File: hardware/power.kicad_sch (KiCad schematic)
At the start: 0 parts

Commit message: train schematics
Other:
- company: Erdapfel -> Frisius
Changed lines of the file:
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@@
   (title_block
     (rev "A")
-    (company "Erdapfel")
+    (company "Frisius")
   )
   (hierarchical_label "VDD_CORE_EN" (shape input) (at 71.755 96.52 180)

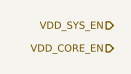
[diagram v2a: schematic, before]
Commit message: usb, bms, proc, btn changes
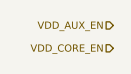
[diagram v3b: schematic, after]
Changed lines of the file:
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@@
     (effects (font (size 0.8 0.8)) (justify right))
   )
-  (hierarchical_label "VDD_SYS_EN" (shape input) (at 71.755 93.98 180)
+  (hierarchical_label "VDD_AUX_EN" (shape input) (at 71.755 93.98 180)
     (effects (font (size 0.8 0.8)) (justify right))
   )

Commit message: started b2b and power
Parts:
- added C? (x2): 4.7u, Capacitor_SMD:C_0603_1608Metric, symbol Device:C_Small
- added C? (x4): 0.1u, Capacitor_SMD:C_0603_1608Metric, symbol Device:C_Small
- added R? (x2): 10k, Resistor_SMD:R_0603_1608Metric, symbol Device:R_Small
- added R? (x2): 0, Resistor_SMD:R_0603_1608Metric, symbol Device:R_Small
- added U? (x2): LK112M33TR, Package_TO_SOT_SMD:SOT-23-5, symbol Regulator_Linear:LK112M33TR
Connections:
- new net: R?.1, U?.1 (SHDN) (x2)
- new net: C?.1, U?.3 (Bypass) (x2)
- new net: C?.1, R?.1, R?.1, R?.2, U?.5 (IN)
- new net GND: C?.2, C?.2, C?.2, C?.2, C?.2, C?.2, U?.2 (GND), U?.2 (GND)
- new net VBUS: R?.2
- new net VBUS_OVP: R?.2
- new net VCC_BKUP_3V3: C?.1, U?.4 (OUT)
- new net VDD_NVDC: C?.1, R?.2, U?.5 (IN)
- new net VDD_USB_3V3: C?.1, U?.4 (OUT)
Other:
- note added: "ISL9113A"
- note added: "NVC8187"
- note added: "Need to reduce 5-12V range to 3.3V, OVP needed, or VBUS from MCP77751 BYP."

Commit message: ready for first review
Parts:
- added C? (x6): 0.1u, Capacitor_SMD:C_0603_1608Metric, symbol Device:C_Small
- added C? (x13): 4.7u, Capacitor_SMD:C_0603_1608Metric, symbol Device:C_Small
- added D?: MBR0540, symbol Device:D_Zener_Small_Filled
- added D? (x3): LED_Small_Filled, symbol Device:LED_Small_Filled
- added L?: L_Small, symbol Device:L_Small
- added R? (x3): 1k, Resistor_SMD:R_0603_1608Metric, symbol Device:R_Small
- added R? (x6): 10k, Resistor_SMD:R_0603_1608Metric, symbol Device:R_Small
- added R?: 180k, Resistor_SMD:R_0603_1608Metric, symbol Device:R_Small
- added U? (x2): NCV8187AMLExCG, Package_DFN_QFN:DFN-8-1EP_3x3mm_P0.65mm_EP1.55x2.4mm, symbol bt_PMIC_Linear:NCV8187AMLExCG
- added U? (x2): PM8903A, Package_DFN_QFN:VQFN-16-1EP_3x3mm_P0.5mm_EP1.45x1.45mm_ThermalVias, symbol bt_PMIC_DCDC_Buck:PM8903A
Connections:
- net 3V3_CORE: now also C?.1, C?.1, D?.2 (A), U?.1 (OUT), U?.2 (SNS/ADJ)
- net GND: now also C?.1, C?.1, C?.2, C?.2, C?.2, C?.2, C?.2, C?.2, C?.2, C?.2, R?.2, R?.2, U?.5 (GND), U?.5 (GND), U?.9 (GND), U?.9 (GND)
- net VCC_BKUP_3V3: now also C?.1, C?.2, U?.12 (VCC)
- net VDD_AUX_3V3: now also C?.1, C?.1, D?.2 (A), U?.1 (OUT), U?.2 (SNS/ADJ)
- net VDD_AUX_EN: now also U?.7 (EN)
- net VDD_CORE_EN: now also D?.1 (K), R?.2, U?.1 (EN)
- net VDD_NVDC: now also C?.1, C?.1, C?.1, U?.13 (VIN), U?.14 (VIN)
- new net: D?.1 (K), R?.1 (x3)
- new net: R?.2, U?.3 (PG) (x2)
- new net: C?.1, C?.2, U?.11 (GND)
- new net: C?.1, R?.1 (x2)
- new net: C?.2, C?.2, R?.1, R?.2, R?.2, U?.10 (FB)
- new net: C?.1, C?.1, C?.1, C?.1, C?.2, C?.2, C?.2, D?.2 (A), L?.2, R?.1, R?.1, R?.2, U?.8 (IN), U?.8 (IN)
- new net: R?.1, U?.7 (EN)
- new net: R?.1, U?.8 (PSKIP/MS)
- new net: C?.1, R?.2, U?.9 (COMP)
- new net: C?.2, L?.1, U?.5 (PHASE), U?.6 (PHASE), U?.7 (PHASE)
- new net: C?.1, U?.4 (BOOT)
- new net: C?.2, C?.2, C?.2, U?.15 (PGND), U?.16 (PGND)
- new net: R?.2, U?.3 (PGOOD)
- new net CORE_BOOTSTRAP: D?.2 (A)
- no-connect marks 0 -> 1
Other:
- note added: "Aux controlled by MCU."
- note added: "Backup regulator always on"
- note added: "Bootstrap allows hard shutdown of core rail, startup via button or other source. Shutdown triggered by ESP pulling low."
- note added: "Core LDO acrive by default."
- note removed: "ISL9113A"
- note removed: "NVC8187"
- moved on the sheet: C?, R?, U?

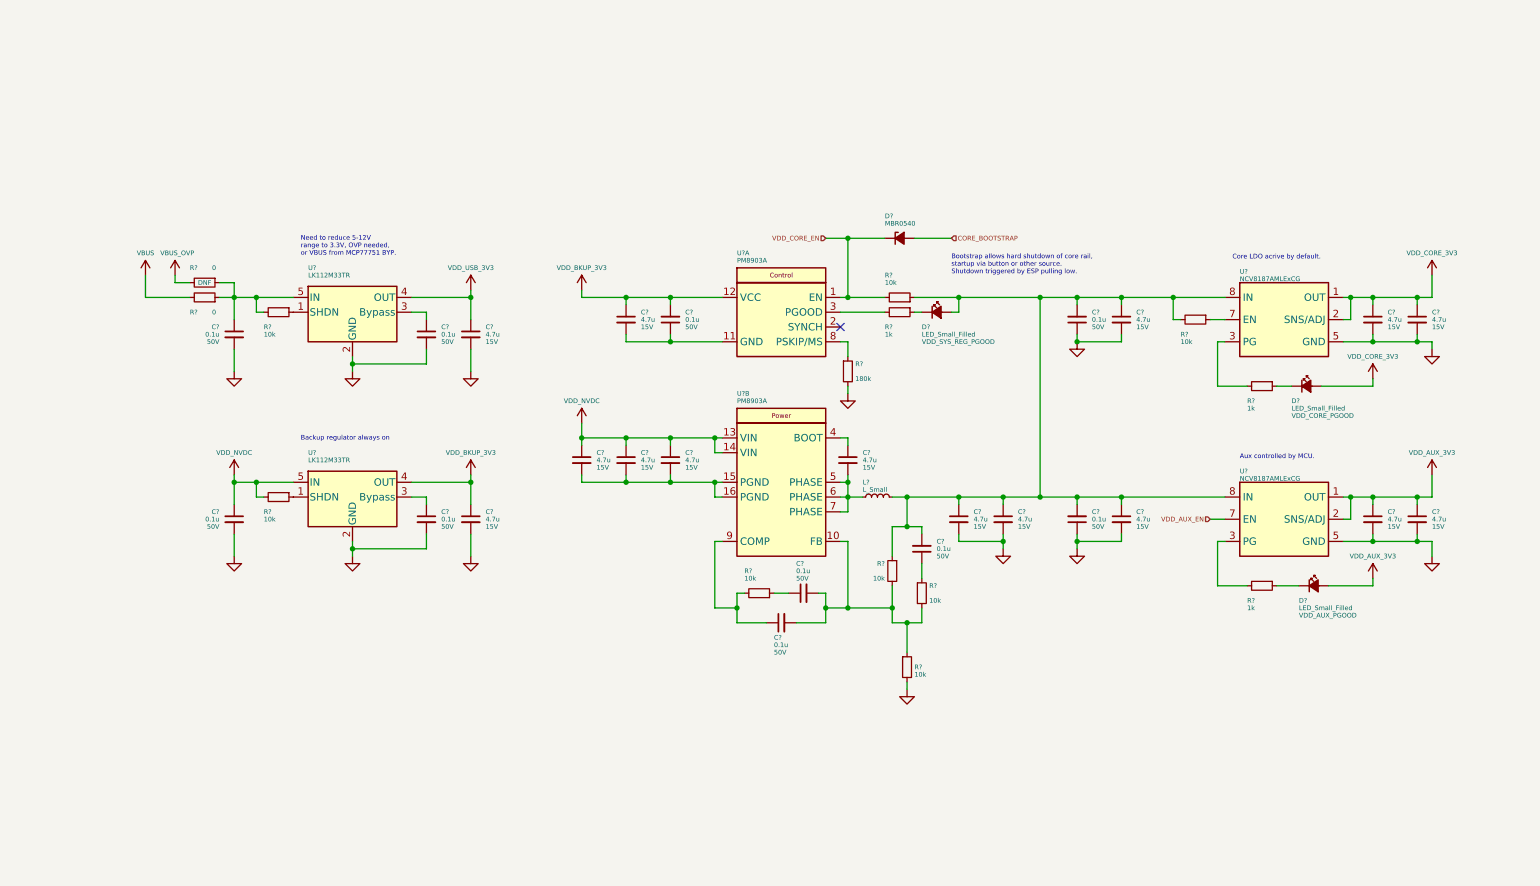
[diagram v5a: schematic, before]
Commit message: checking footprint assignment, added current sense pac1934 for dev
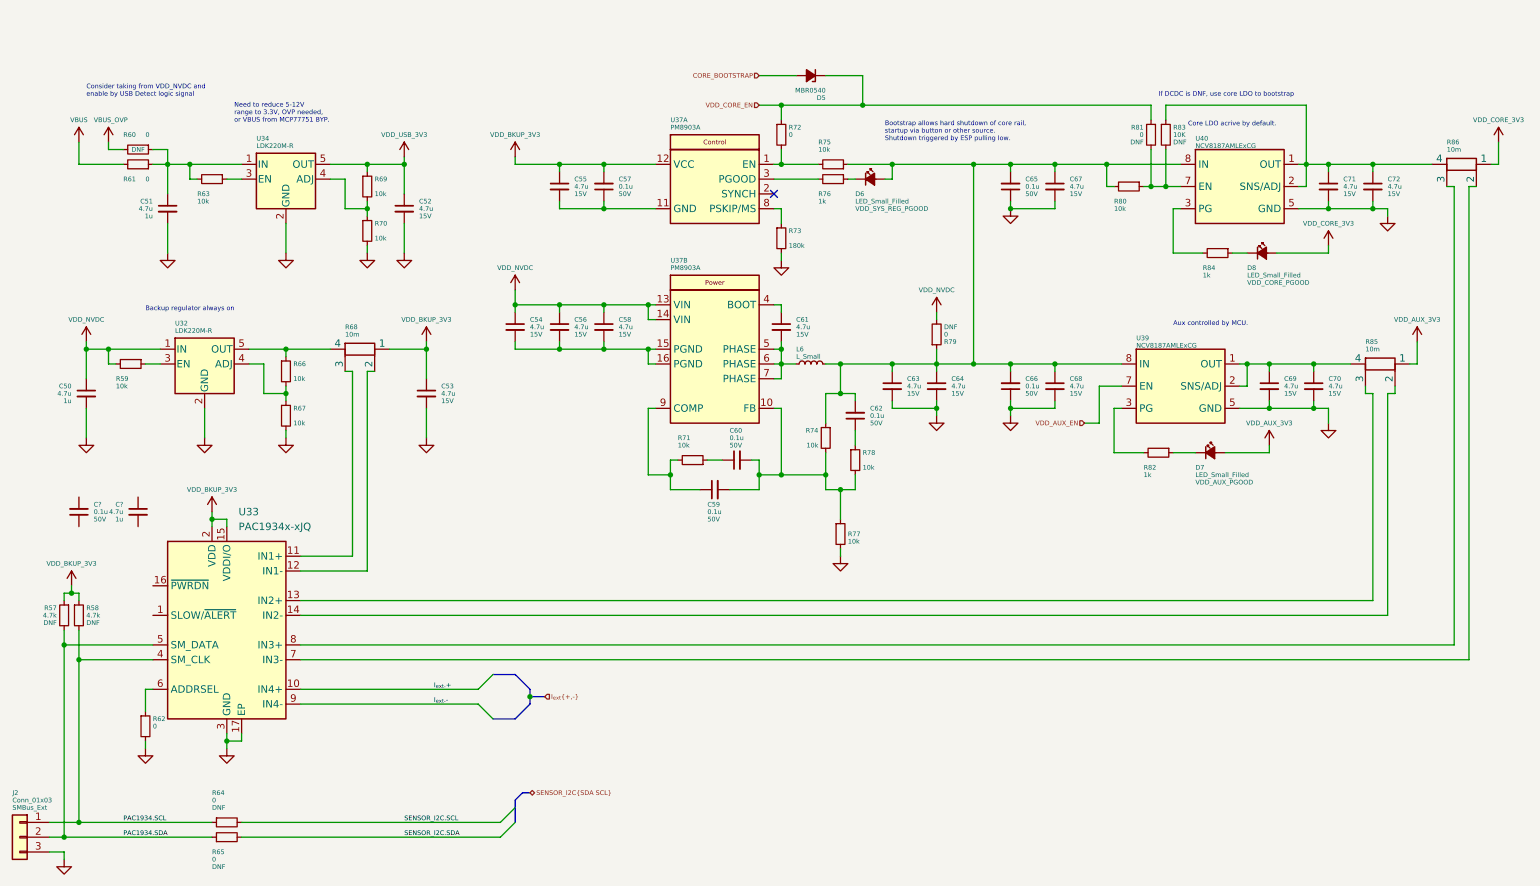
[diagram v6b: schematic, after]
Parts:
- removed C?: 4.7u, Capacitor_SMD:C_0603_1608Metric, symbol Device:C_Small
- removed C? (x4): 0.1u, Capacitor_SMD:C_0603_1608Metric, symbol Device:C_Small
- removed R?: 10k, Resistor_SMD:R_0603_1608Metric, symbol Device:R_Small
- removed U? (x2): LK112M33TR, Package_TO_SOT_SMD:SOT-23-5, symbol Regulator_Linear:LK112M33TR
- added C50, C51, C53, C?: 4.7u, Capacitor_SMD:C_0603_1608Metric, symbol Device:C_Small
- added C?: 0.1u, Capacitor_SMD:C_0603_1608Metric, symbol Device:C_Small
- added J2: Conn_01x03, Connector_PinHeader_1.00mm:PinHeader_1x03_P1.00mm_Vertical, symbol Connector_Generic:Conn_01x03
- added R57, R58: 4.7k, Resistor_SMD:R_0603_1608Metric, symbol Device:R_Small
- added R59, R66, R67, R69, R70: 10k, Resistor_SMD:R_0603_1608Metric, symbol Device:R_Small
- added R62, R64, R65, R72, R79, R81: 0, Resistor_SMD:R_0603_1608Metric, symbol Device:R_Small
- added R68, R85, R86: 10m, Resistor_SMD:R_1210_3225Metric, symbol Device:R_Shunt
- added R83: 10K, Resistor_SMD:R_0603_1608Metric, symbol Device:R_Small
- added U32, U34: LDK220M-R, Package_TO_SOT_SMD:SOT-23-5, symbol Regulator_Linear:LDK130-ADJ_SOT23_SOT353
- added U33: PAC1934x-xJQ, Package_DFN_QFN:UQFN-16-1EP_4x4mm_P0.65mm_EP2.7x2.7mm, symbol Analog_ADC:PAC1934x-xJQ
- D5: renamed from D?; footprint (none) -> Diode_SMD:D_0603_1608Metric
- D6, D7, D8: renamed from D?; footprint (none) -> LED_SMD:LED_0603_1608Metric
- L6: renamed from L?; footprint (none) -> Inductor_SMD:L_Bourns-SRN4018
- gave numbers to parts that had none: 36
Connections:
- net 3V3_CORE: now also R86.1; no longer C71.1, C72.1, U40.1 (OUT), U40.2 (SNS/ADJ)
- net GND: now also C50.2, C51.2, C53.2, J2.3 (Pin_3), R62.2, R67.2, R70.2, U32.2 (GND), U33.17 (EP), U33.3 (GND), U34.2 (GND)
- net VCC_BKUP_3V3: now also C53.1, R57.1, R58.1, R68.1, U33.15 (VDDI/O), U33.2 (VDD)
- net VDD_AUX_3V3: now also R85.1; no longer C69.1, C70.1, U39.1 (OUT), U39.2 (SNS/ADJ)
- net VDD_CORE_EN: now also R72.1, R81.1; no longer R75.2, U37.1 (EN)
- net VDD_NVDC: now also C50.1, R59.2, R79.2, U32.1 (IN)
- net VDD_USB_3V3: now also R69.1, U34.5 (OUT)
- net at C62.2, C63.1, C64.1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: now also R79.1
- net at R63.1: now also U34.3 (EN)
- net at R60.1, R61.1, R63.2: now also C51.1, U34.1 (IN)
- net at R80.1, U40.7 (EN): now also R81.2, R83.2
- new net: C71.1, C72.1, R83.1, R86.4, U40.1 (OUT), U40.2 (SNS/ADJ)
- new net: R72.2, R75.2, U37.1 (EN)
- new net: R66.1, R68.4, U32.5 (OUT)
- new net: R66.2, R67.1, U32.4 (ADJ)
- new net: R68.2, U33.12 (IN1-)
- new net: R68.3, U33.11 (IN1+)
- new net: C69.1, C70.1, R85.4, U39.1 (OUT), U39.2 (SNS/ADJ)
- new net: R85.3, U33.13 (IN2+)
- new net: R85.2, U33.14 (IN2-)
- new net: R62.1, U33.6 (ADDRSEL)
- new net: R86.2, U33.7 (IN3-)
- new net: R86.3, U33.8 (IN3+)
- new net: R69.2, R70.1, U34.4 (ADJ)
- new net: R59.1, U32.3 (EN)
- new net I_{ext}.+: U33.10 (IN4+)
- new net I_{ext}.-: U33.9 (IN4-)
- new net PAC1934.SCL: J2.1 (Pin_1), R58.2, R64.1, U33.4 (SM_CLK)
- new net PAC1934.SDA: J2.2 (Pin_2), R57.2, R65.1, U33.5 (SM_DATA)
- new net SENSOR_I2C.SCL: R64.2
- new net SENSOR_I2C.SDA: R65.2
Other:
- note added: "Consider taking from VDD_NVDC and enable by USB Detect logic signal"
- note added: "If DCDC is DNF, use core LDO to bootstrap"
- moved on the sheet: C52, C54, C55, C56, C57, C58, C59, C60, C61, C62, C63, C64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

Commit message: hardware update
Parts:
- removed C53, C54, C55, C56, C58, C61, C63, C64, C67, C68, C69, C70, C71, C72, C?: 4.7u, Capacitor_SMD:C_0603_1608Metric, symbol Device:C_Small
- removed C57, C59, C60, C62, C65, C66: 0.1u, Capacitor_SMD:C_0603_1608Metric, symbol Device:C_Small
- removed D5: MBR0540, Diode_SMD:D_0603_1608Metric, symbol Device:D_Zener_Small_Filled
- removed D6: LED_Small_Filled, LED_SMD:LED_0603_1608Metric, symbol Device:LED_Small_Filled
- removed J2: Conn_01x03, Connector_PinHeader_1.00mm:PinHeader_1x03_P1.00mm_Vertical, symbol Connector_Generic:Conn_01x03
- removed L6: L_Small, Inductor_SMD:L_Bourns-SRN4018, symbol Device:L_Small
- removed R57, R58: 4.7k, Resistor_SMD:R_0603_1608Metric, symbol Device:R_Small
- removed R59, R63, R66, R67, R69, R70, R71, R74, R77, R78, R80: 10k, Resistor_SMD:R_0603_1608Metric, symbol Device:R_Small
- removed R60, R61, R62, R64, R65, R72, R79, R81: 0, Resistor_SMD:R_0603_1608Metric, symbol Device:R_Small
- removed R73: 180k, Resistor_SMD:R_0603_1608Metric, symbol Device:R_Small
- removed R76, R82, R84: 1k, Resistor_SMD:R_0603_1608Metric, symbol Device:R_Small
- removed R83: 10K, Resistor_SMD:R_0603_1608Metric, symbol Device:R_Small
- removed R85, R86: 10m, Resistor_SMD:R_1210_3225Metric, symbol Device:R_Shunt
- removed U32, U34: LDK220M-R, Package_TO_SOT_SMD:SOT-23-5, symbol Regulator_Linear:LDK130-ADJ_SOT23_SOT353
- removed U37: PM8903A, Package_DFN_QFN:VQFN-16-1EP_3x3mm_P0.5mm_EP1.45x1.45mm_ThermalVias, symbol bt_PMIC_DCDC_Buck:PM8903A
- removed U39, U40: NCV8187AMLExCG, Package_DFN_QFN:DFN-8-1EP_3x3mm_P0.65mm_EP1.55x2.4mm, symbol bt_PMIC_Linear:NCV8187AMLExCG
- added C43, C46: 4.7u, Capacitor_SMD:C_0603_1608Metric, symbol Device:C_Small
- added C45: 1u, Capacitor_SMD:C_0603_1608Metric, symbol Device:C_Small
- added C47: 10p, Capacitor_SMD:C_0402_1005Metric, symbol Device:C_Small
- added C48, C49: 10u, Capacitor_SMD:C_0805_2012Metric, symbol Device:C_Small
- added C50: 0.1u, Capacitor_SMD:C_0402_1005Metric, symbol Device:C_Small
- added D6: MBR0540, LED_SMD:LED_0603_1608Metric, symbol Device:D_Zener_Small_Filled
- added L4: 1u, Inductor_SMD:L_Wuerth_MAPI-2510, symbol Device:L_Small
- added Q3, Q4: Q_NMOS_DGS, Package_TO_SOT_SMD:SOT-323_SC-70, symbol Device:Q_NMOS_DGS
- added R34, R35, R38, R42: 100k, Resistor_SMD:R_0402_1005Metric, symbol Device:R_Small
- added R37: ?, Resistor_SMD:R_0402_1005Metric, symbol Device:R_Small
- added R40: 10m, Resistor_SMD:R_0603_1608Metric_Pad0.98x0.95mm_HandSolder, symbol Device:R_Shunt
- added R41, R44: 1k, Resistor_SMD:R_0402_1005Metric, symbol Device:R_Small
- added R43: 10m, Resistor_SMD:R_0603_1608Metric, symbol Device:R_Shunt
- added U12: RT5789, Package_DFN_QFN:DFN-10-1EP_3x3mm_P0.5mm_EP1.55x2.48mm, symbol bt_PMIC_DCDC_Buck:RT5789
- added U13: MAX8881EUT33+T, Package_TO_SOT_SMD:SOT-23-6, symbol bt_PMIC_Linear:MAX8881EUT33+T
- added U15: AP228X4BSN, bt_Package_DFN:Diodes_UDFN2020-6, symbol bt_Power_Management:AP228X4BSN
- C42: renamed from C?; footprint Capacitor_SMD:C_0603_1608Metric -> Capacitor_SMD:C_0402_1005Metric
- C44: renamed from C50; value 4.7u -> 1u; Voltage 1u -> 15V
- C51: value 4.7u -> 10u; footprint Capacitor_SMD:C_0603_1608Metric -> Capacitor_SMD:C_0805_2012Metric; Voltage 1u -> 25V
- C52: value 4.7u -> 10u; footprint Capacitor_SMD:C_0603_1608Metric -> Capacitor_SMD:C_0805_2012Metric; Voltage 15V -> 25V
- D7: Label VDD_AUX_PGOOD -> VDD_CORE_OK
- D8: Label VDD_CORE_PGOOD -> VDD_AUX_OK
- R36: renamed from R75; value 10k -> 100k; footprint Resistor_SMD:R_0603_1608Metric -> Resistor_SMD:R_0402_1005Metric
- R39: renamed from R68; footprint Resistor_SMD:R_1210_3225Metric -> Resistor_SMD:R_0603_1608Metric_Pad0.98x0.95mm_HandSolder
- renumbered U33 to U14
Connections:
- net PAC1934.SCL is gone; now on net SENSOR_I2C.SCL: U14.4 (SM_CLK)
- net PAC1934.SDA is gone; now on net SENSOR_I2C.SDA: U14.5 (SM_DATA)
- net VDD_USB_3V3 is gone; now on an unnamed net: C52.1
- net 3V3_CORE: now also D7.2 (A), R40.1; no longer D8.2 (A)
- net GND: now also C42.1, U14.6 (ADDRSEL), C43.2, C45.2, C46.2, C48.2, C49.2, C50.1, Q3.3 (S), Q4.3 (S), R38.2, R41.1, R44.1, U12.2 (VIN), U12.6 (AGND), U13.2 (GND), U15.2 (GND)
- net VCC_BKUP_3V3: now also C42.2, R34.1, R35.1
- net VDD_AUX_3V3: now also D8.2 (A), R43.1; no longer D7.2 (A)
- net VDD_NVDC: now also C43.1, C45.1, U12.2 (VIN), U13.1 (IN), U13.5 (EN)
- net at D8.1 (K): now also R44.2
- net VDD_SYS_3V3: now reaches R36.1
- net VDD_SYS_3V3: now also C47.1, C48.1, C49.1, C50.2, L4.2, R37.1, R40.4, R42.1, U12.5 (VOUT), U15.1 (IN)
- net PWR_CTRL.CORE_EN: now reaches R36.2
- net PWR_CTRL.CORE_EN: now also D6.1 (K), Q3.2 (G), U12.8 (EN)
- net at R39.4: now also C46.1, U13.3 (OUT), U13.4 (FB)
- net at C51.1: now also R43.4, U15.5 (OUT)
- net at D7.1 (K): now also R41.2
- net at U14.1 (SLOW/~{ALERT}): now also Q3.1 (D), R34.2
- net at U14.13 (IN2+): now also R40.3
- net at U14.14 (IN2-): now also R40.2
- net at U14.16 (~{PWRDN}): now also R35.2
- net at U14.7 (IN3-): now also R43.2
- net at U14.8 (IN3+): now also R43.3
- net I_{ext}.+ renamed I_{bat}.+
- net I_{ext}.- renamed I_{bat}.-
- new net: L4.1, U12.3 (LX)
- new net: Q4.1 (D), R42.2, U15.3 (~{EN})
- new net: C47.2, R37.2, R38.1, U12.7 (FB)
- new net BOOTSTRAP: D6.2 (A)
- new net PWR_CTRL.AUX_EN: Q4.2 (G)
- no-connect marks 1 -> 2
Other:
- note added: "External channel to cell"
- note added: "Kelvin traces to sense resistors, keep short"
- note removed: "Aux controlled by MCU."
- note removed: "Consider taking from VDD_NVDC and enable by USB Detect logic signal"
- note removed: "Core LDO acrive by default."
- note removed: "If DCDC is DNF, use core LDO to bootstrap"
- note removed: "Need to reduce 5-12V range to 3.3V, OVP needed, or VBUS from MCP77751 BYP."
- moved on the sheet: C42, C44, R36, R39, U14

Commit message: initial component placement and design simplification
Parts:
- removed C42, C50: 0.1u, Capacitor_SMD:C_0402_1005Metric, symbol Device:C_Small
- removed C51, C52: 10u, Capacitor_SMD:C_0805_2012Metric, symbol Device:C_Small
- removed D8: LED_Small_Filled, LED_SMD:LED_0603_1608Metric, symbol Device:LED_Small_Filled
- removed Q3, Q4: Q_NMOS_DGS, Package_TO_SOT_SMD:SOT-323_SC-70, symbol Device:Q_NMOS_DGS
- removed R34, R35, R42: 100k, Resistor_SMD:R_0402_1005Metric, symbol Device:R_Small
- removed R39, R40: 10m, Resistor_SMD:R_0603_1608Metric_Pad0.98x0.95mm_HandSolder, symbol Device:R_Shunt
- removed R43: 10m, Resistor_SMD:R_0603_1608Metric, symbol Device:R_Shunt
- removed R44: 1k, Resistor_SMD:R_0402_1005Metric, symbol Device:R_Small
- removed U14: PAC1934x-xJQ, Package_DFN_QFN:UQFN-16-1EP_4x4mm_P0.65mm_EP2.7x2.7mm, symbol Analog_ADC:PAC1934x-xJQ
- removed U15: AP228X4BSN, bt_Package_DFN:Diodes_UDFN2020-6, symbol bt_Power_Management:AP228X4BSN
- added R39, R40, R43: 0, Resistor_SMD:R_0603_1608Metric_Pad0.98x0.95mm_HandSolder, symbol Device:R_Small
- U12: footprint Package_DFN_QFN:DFN-10-1EP_3x3mm_P0.5mm_EP1.55x2.48mm -> Package_TO_SOT_SMD:TSOT-23-8
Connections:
- net 3V3_CORE: now also R40.2
- net GND: now also U12.4 (PGND); no longer U12.2 (VIN)
- net VCC_BKUP_3V3: now also R39.2
- net VDD_AUX_3V3: now also R43.2
- net VDD_SYS_3V3: now also R40.1, R43.1
- net at C46.1, U13.3 (OUT), U13.4 (FB): now also R39.1
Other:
- note removed: "External channel to cell"
- note removed: "Kelvin traces to sense resistors, keep short"
